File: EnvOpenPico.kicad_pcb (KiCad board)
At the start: 2 copper layers, 21.1 x 51.3 mm, 33 parts, among them J2 Conn_01x02, J3 Conn_02x18_Odd_Even, J4 Conn_02x18_Odd_Even, J5 Conn_01x03_Male, U1 NCP1117-3.3_SOT223, U2 W25Q16JVSSIQ, U3 RP2040, X1 XO32

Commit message: Updated image
sleep deprivation lol.
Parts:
- moved X1 3.88 mm to (85.9, 87.6)
- moved C2 3.08 mm to (87.3, 85.7), turned to 180 degrees
- moved C15 1.82 mm to (85.1, 85.6)
- moved C14 0.25 mm to (90.2, 83.7)
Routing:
- net /XIN: track 11.1 -> 7.62 mm
- net +3V3: track 66.5 -> 64.4 mm
- net /XOUT: track 1.57 -> 0.00 mm
- net GND: track 46.2 -> 45.6 mm

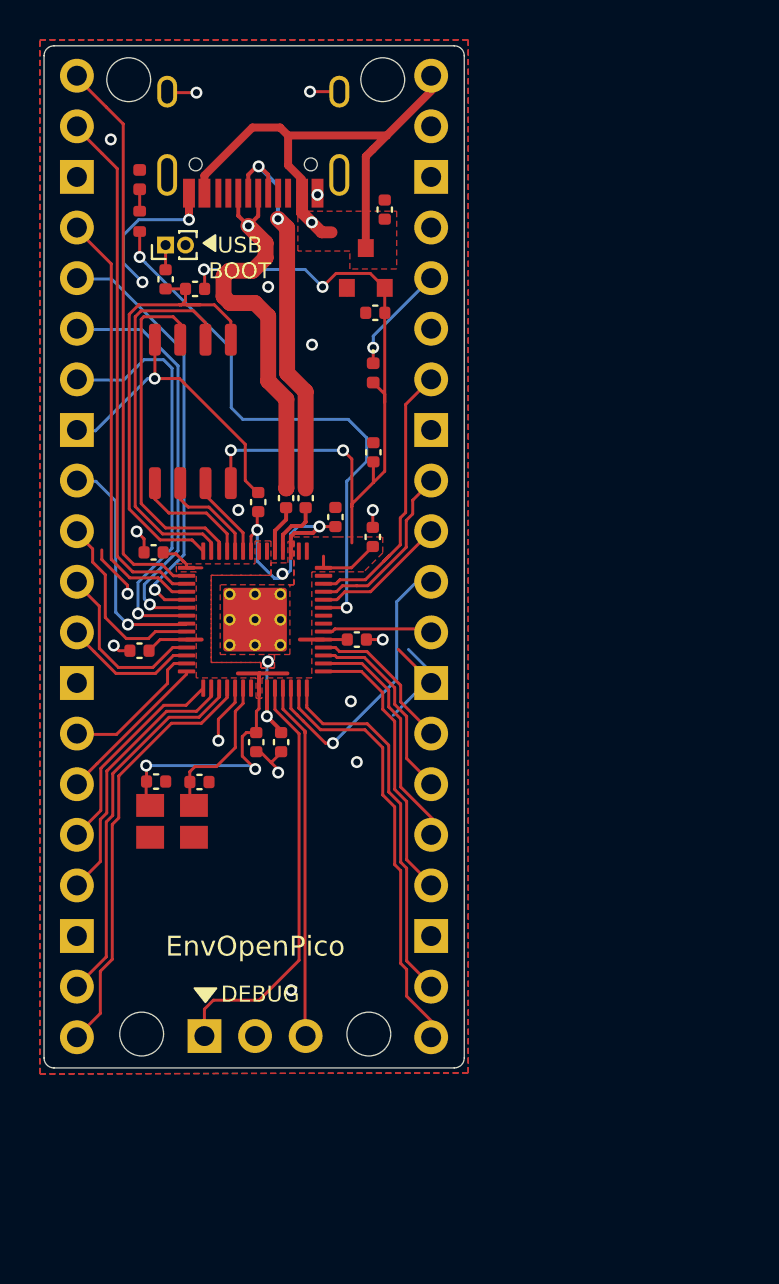
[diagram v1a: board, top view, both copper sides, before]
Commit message: Changed Regulator for one with an enable pin
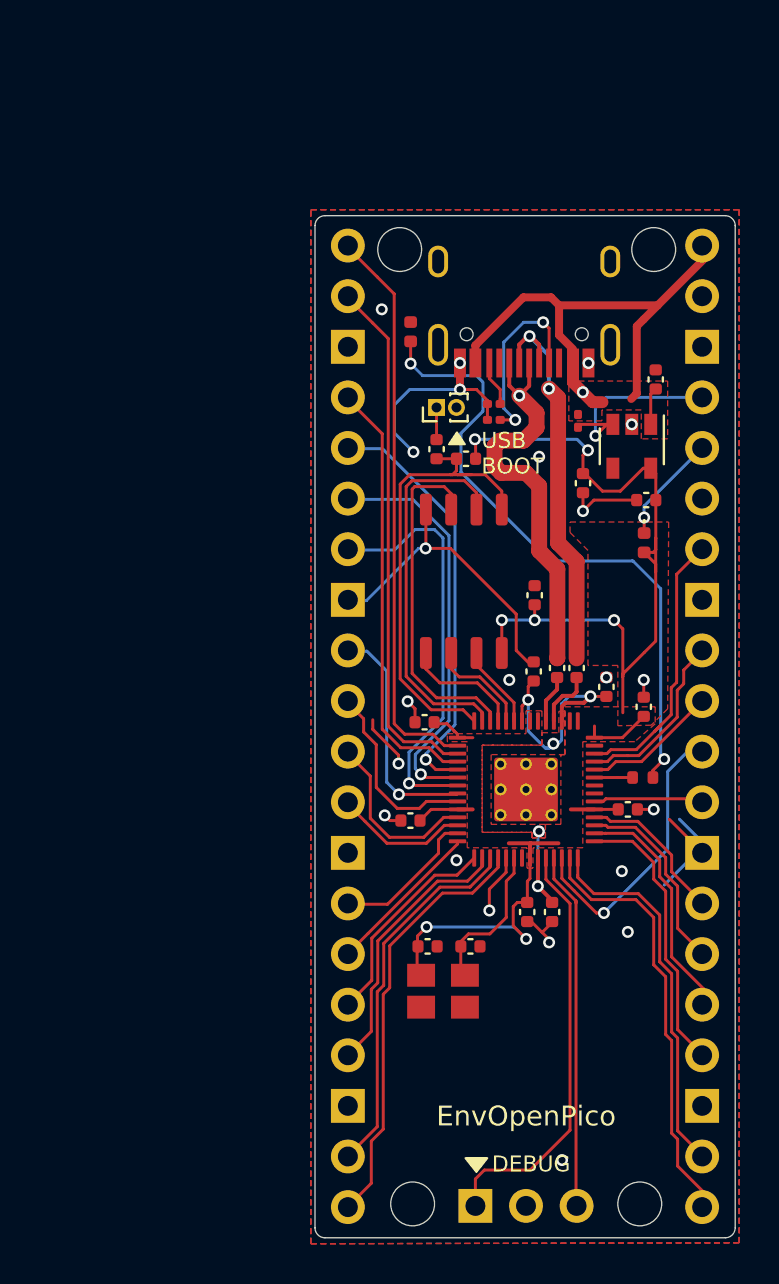
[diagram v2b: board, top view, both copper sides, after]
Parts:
- added C4: 10u, Capacitor_SMD:C_0402_1005Metric, F.Cu at (109.7, 71.5)
- added R5: 5.1K, Resistor_SMD:R_0201_0603Metric, F.Cu at (102.1, 67.5)
- added R6: 5.1K, Resistor_SMD:R_0201_0603Metric, F.Cu at (102.1, 66.7)
- added R7: R100K, Resistor_SMD:R_0201_0603Metric, F.Cu at (106.3, 67.5)
- U1: value NCP1117-3.3_SOT223 -> SPX3819M5-L-3-3; footprint Package_TO_SOT_SMD:SOT-23 -> Package_TO_SOT_SMD:SOT-23-5
- moved R8 37.6 mm to (109.5, 85.4), turned to 180 degrees
- moved C10 23.9 mm to (109.6, 81.9), turned to 90 degrees
- moved C3 16.2 mm to (104.1, 80.1)
- moved U1 16.1 mm to (109.0, 68.8), turned to 270 degrees
- moved D2 16.1 mm to (109.6, 73.6)
- moved H3 16.1 mm to (109.4, 106.8)
- moved X1 16.1 mm to (99.5, 96.2)
- moved C1 16.1 mm to (110.2, 65.4)
- moved J5 16.1 mm to (101.2, 106.9)
- moved R1 16.1 mm to (99.2, 68.9)
- moved R2 16.1 mm to (100.7, 69.4)
- moved R4 16.1 mm to (106.2, 79.9)
- moved C11 16.1 mm to (98.6, 82.7)
- moved C13 16.1 mm to (108.8, 87.0)
- moved C7 16.1 mm to (107.7, 80.9)
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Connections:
- J4 pad 4: Net-(J4-Pad4) -> 3V3_EN
- U1 pad 1: GND -> VBUS
- U1 pad 2: +3V3 -> GND
- U1 pad 3: VBUS -> 3V3_EN
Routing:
- net Net-(D3-Pad2): track 1.10 -> 32.3 mm, vias 0 -> 2
- net /GPIO25: track 28.3 -> 1.91 mm, vias 2 -> 0
- net 3V3_EN: track 0.00 -> 10.5 mm, vias 0 -> 1
- net Net-(R5-Pad2): track 0.00 -> 9.45 mm, vias 0 -> 2
- net GND: track 45.6 -> 48.9 mm, vias 20 -> 22
- net Net-(R6-Pad2): track 0.00 -> 2.56 mm
- net +3V3: track 64.4 -> 66.5 mm, vias 6 -> 7
- net VBUS: track 27.8 -> 28.8 mm

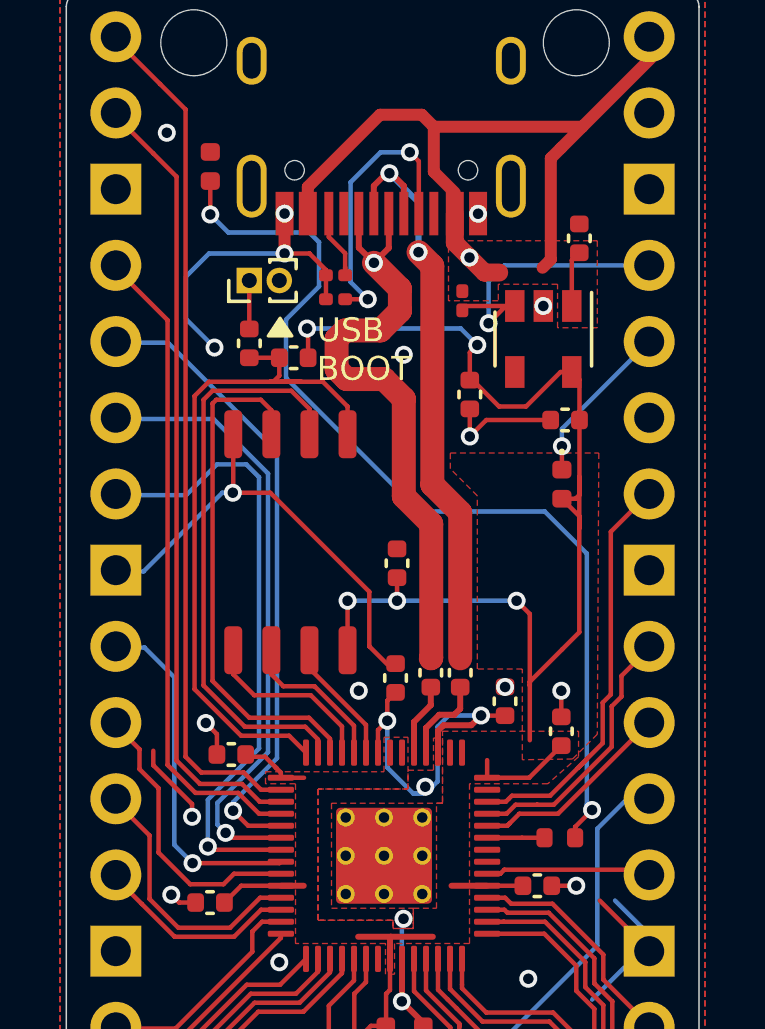
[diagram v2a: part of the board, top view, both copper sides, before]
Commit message: Changed SOIC Flash for WSON Flash
also added a button instead of 1mm pitch headers along with general other track adjustments and stuff.
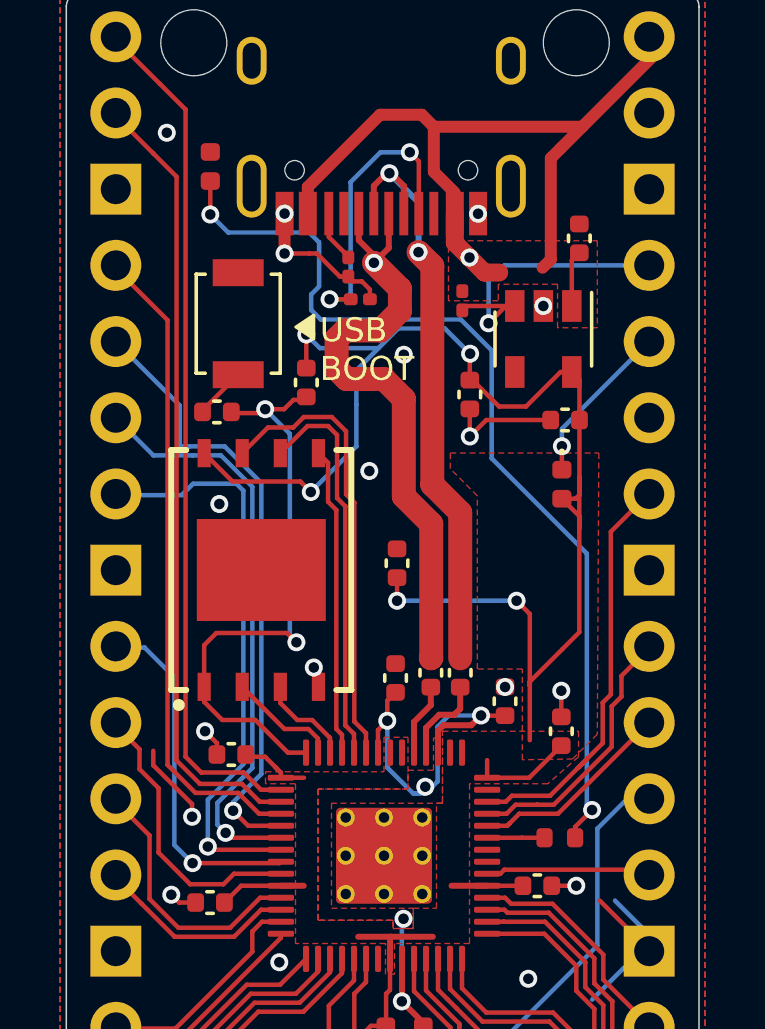
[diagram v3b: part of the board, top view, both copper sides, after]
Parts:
- J2: footprint Connector_PinHeader_1.00mm:PinHeader_1x02_P1.00mm_Vertical -> Button_Switch_SMD:SW_SPST_B3U-1000P
- U2: value W25Q16JVSSIQ -> W25Q256JVEIQ_TR; footprint Package_SO:SOIC-8_5.23x5.23mm_P1.27mm -> W25Q256JVEIQ_TR:SON127P800X600X80-9N
- moved R1 2.53 mm to (98.1, 71.2), turned to 180 degrees
- moved J2 1.49 mm to (98.8, 68.3)
- moved U2 1.34 mm to (99.6, 76.5), turned to 90 degrees
- moved R2 0.93 mm to (101.1, 70.2), turned to 270 degrees
- moved R5 0.83 mm to (102.9, 67.5), turned to 180 degrees
- moved R6 0.51 mm to (102.5, 66.4), turned to 90 degrees
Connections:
- J4 pad 2: Net-(J4-Pad2) -> (no net)
- J4 pad 6: Net-(J4-Pad6) -> (no net)
- U1 pad 4: Net-(U1-Pad4) -> (no net)
- U3 pad 21: /XOUT -> (no net)
- U3 pad 35: /GPIO23 -> (no net)
- U3 pad 36: /GPIO24 -> (no net)
- U3 pad 41: /GPIO29_ADC3 -> (no net)
- X1 pad 1: Net-(X1-Pad1) -> (no net)
- e1 pad 3: Net-(e1-Pad3) -> (no net)
- e1 pad 9: Net-(e1-Pad9) -> (no net)
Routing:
- net GND: track 48.9 -> 27.8 mm
- net /QSPI_SD1: track 19.3 -> 3.71 mm
- net /QSPI_SD2: track 17.4 -> 3.17 mm
- net /QSPI_SD3: track 4.19 -> 15.1 mm
- net /QSPI_SCLK: track 5.16 -> 13.2 mm
- net +3V3: track 66.5 -> 73.1 mm
- net /QSPI_SD0: track 6.02 -> 10.3 mm
- net /QSPI_SS: track 23.6 -> 20.2 mm, vias 0 -> 2
- net /GPIO5: track 20.9 -> 19.4 mm
- net /GPIO4: track 20.6 -> 19.5 mm
- net Net-(R6-Pad2): track 2.56 -> 1.78 mm
- net /GPIO3: track 21.3 -> 20.7 mm

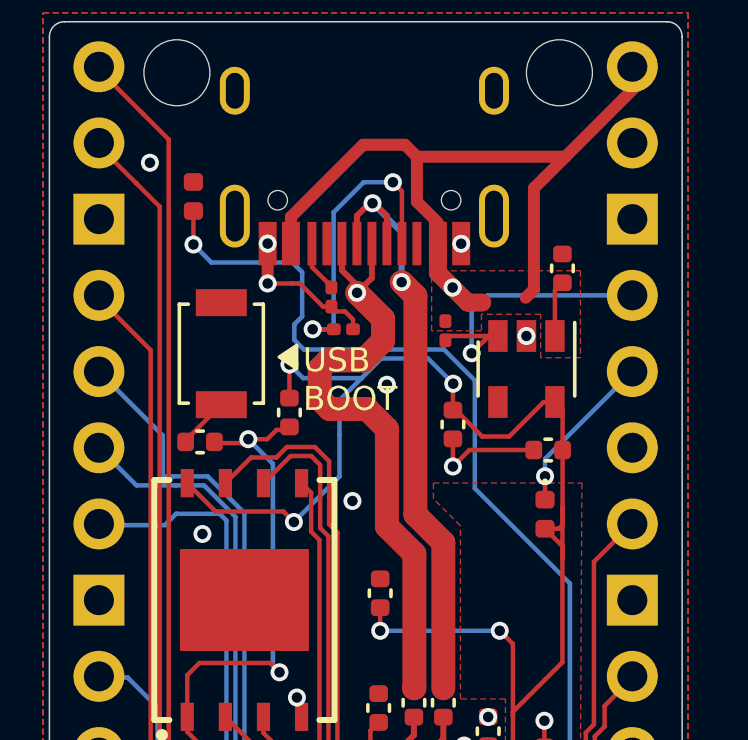
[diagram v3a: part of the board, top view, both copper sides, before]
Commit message: Updated some components to be JLCPCB SMT Assembly compatible
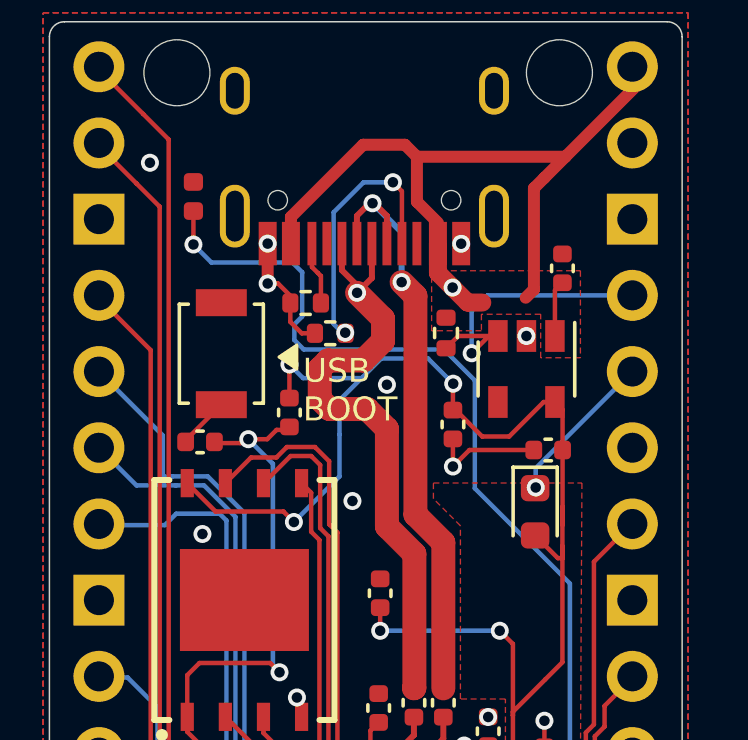
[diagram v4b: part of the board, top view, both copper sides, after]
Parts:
- D2: footprint Diode_SMD:D_0402_1005Metric -> Diode_SMD:D_0603_1608Metric
- R5, R6, R7: footprint Resistor_SMD:R_0201_0603Metric -> Resistor_SMD:R_0402_1005Metric
- moved R6 0.88 mm to (101.6, 66.6), turned to 0 degrees
- moved R5 0.46 mm to (102.5, 67.6), turned to 0 degrees
- moved D2 0.34 mm to (109.3, 73.6)
- moved R7 0.08 mm to (106.3, 67.6)
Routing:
- net Net-(R5-Pad2): track 9.76 -> 8.79 mm
- net GND: track 27.8 -> 26.9 mm

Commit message: Some general changes and house keeping
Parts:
- added G***: LOGO, EnvExtras:logo, F.Cu at (103.7, 101.2)

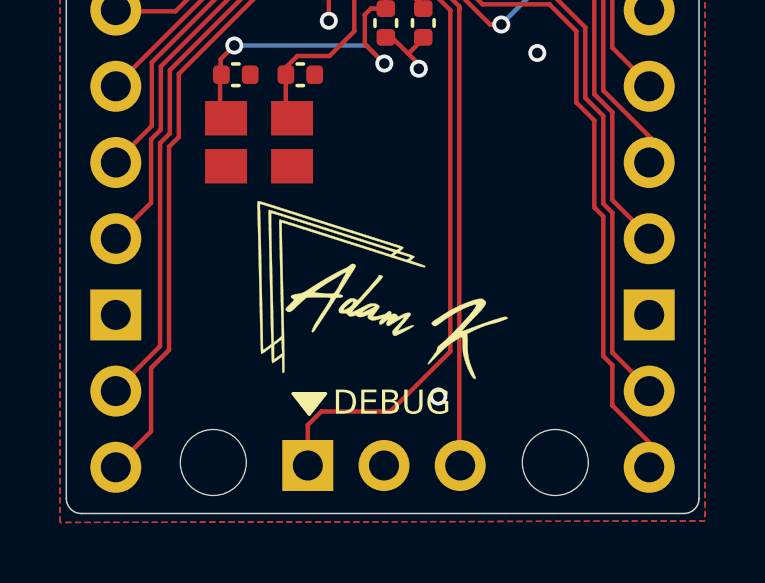
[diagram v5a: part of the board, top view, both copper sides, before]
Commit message: some silkscreen adjustments and a couple added notes to schematic
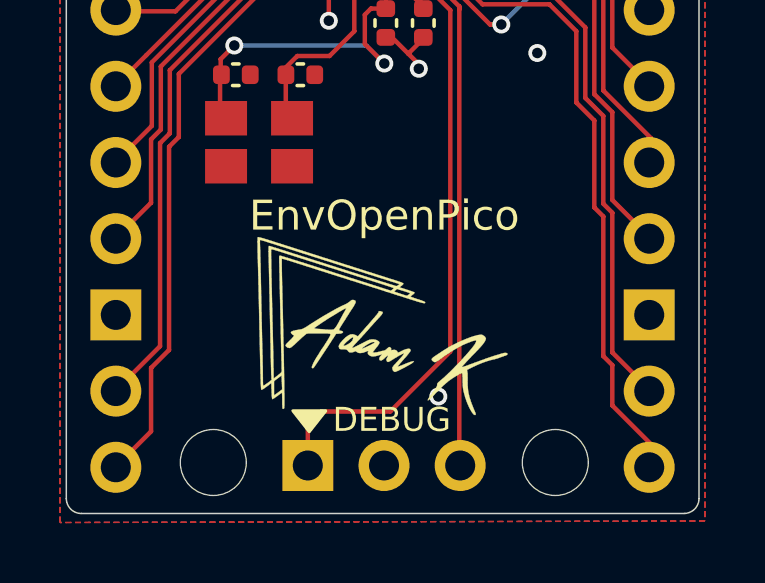
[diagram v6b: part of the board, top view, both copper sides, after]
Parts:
- moved G*** 1.20 mm to (103.7, 102.4)
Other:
- board text added: "PROTOTYPE"
- board text added: "REV#0"

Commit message: Updated Gerber Files
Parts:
- removed G***: LOGO, EnvExtras:logo

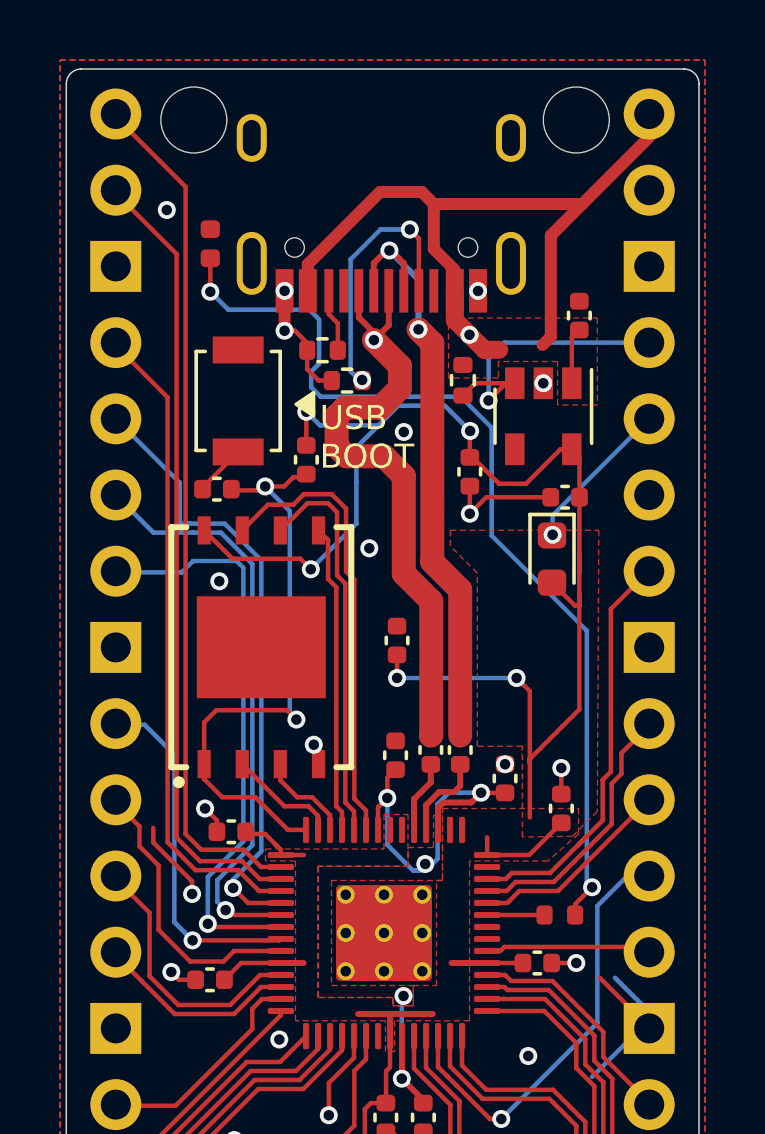
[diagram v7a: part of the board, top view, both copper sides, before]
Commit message: some more adjustments to correct auto filling fields in JLCPCB
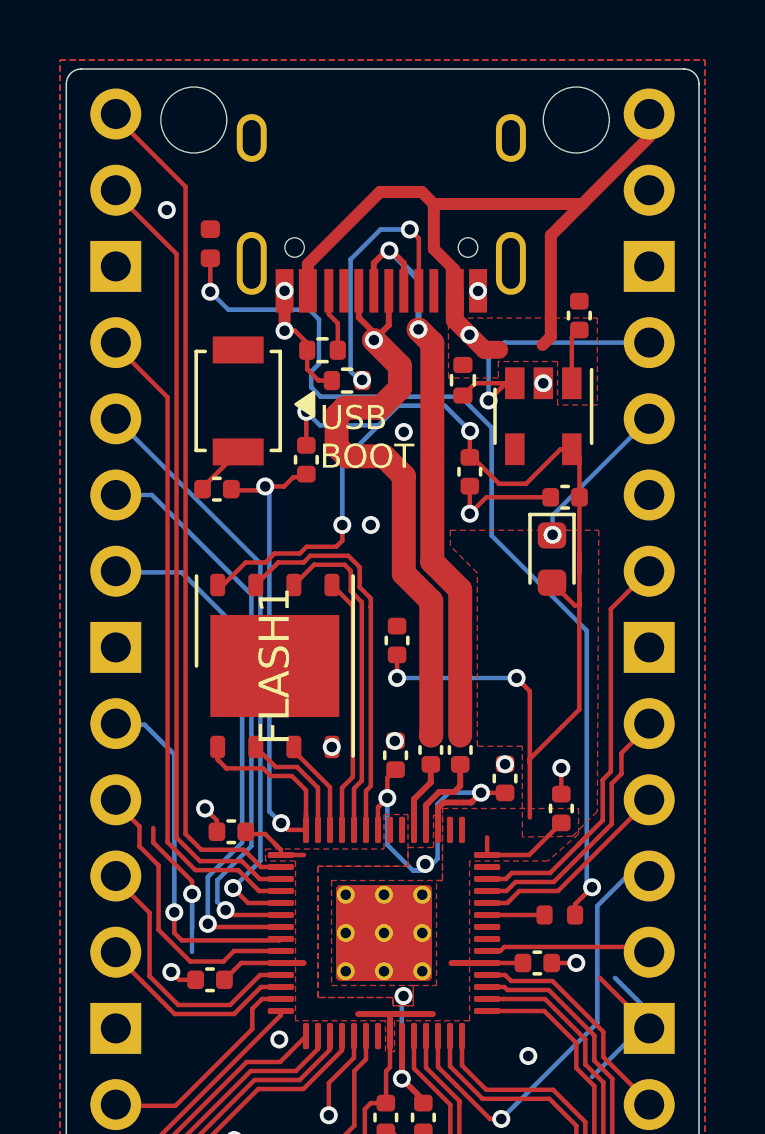
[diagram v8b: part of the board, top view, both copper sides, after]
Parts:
- removed U2: W25Q256JVEIQ_TR, W25Q256JVEIQ_TR:SON127P800X600X80-9N
- added FLASH1: W25Q128JVPIQ, Package_SON:WSON-8-1EP_6x5mm_P1.27mm_EP3.4x4.3mm, F.Cu at (100.0, 77.1)
- D2: value D_Schottky -> 0603 Diode 1N58
- D3: value GPIO25 LED -> LED 0402 YELLOW
- J2: value Conn_01x02 -> B3U-1000P
- J3, J4: value Conn_02x18_Odd_Even -> 2.54mm header 01x20
- R3, R4: value 27 -> 27Ohms 0402 Resistor
- R7: value R100K -> 100K
- R8: value R470 -> 470
- X1: value XO32 -> XO 32 12Mhz 3225 seiko
- e1: value USB_C -> TYPE-C-31-M-12
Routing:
- net /QSPI_SD3: track 15.1 -> 13.0 mm
- net /QSPI_SCLK: track 13.2 -> 11.2 mm
- net GND: track 26.9 -> 28.8 mm
- net /QSPI_SD0: track 10.3 -> 8.60 mm
- net /GPIO5: track 19.4 -> 17.8 mm
- net /GPIO3: track 20.7 -> 19.8 mm
- net +3V3: track 72.9 -> 72.2 mm
- net VBUS: track 28.8 -> 29.4 mm
- net /GPIO4: track 19.5 -> 18.9 mm
- net /QSPI_SS: track 20.2 -> 20.7 mm
